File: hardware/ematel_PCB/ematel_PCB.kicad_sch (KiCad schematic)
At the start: 138 parts, among them J1 V_USB, J10 Micro_SD_Card, J11 HDR-4x1, J12 HDR-2x1, J13 HDR-2x1, J14 HDR-2x1, J15 HDR-2x1, J16 HDR-2x1, J17 USB_B_Micro, J2 BAT, J3 HDR-2x1, J4 IN, J5 HDR-3x1, J6 HDR-3x1, J7 IN, J8 HDR-2x1, J9 Conn_01x02, Q1 Q_PMOS_GSD, Q2 Q_PMOS_GSD, Q3 Q_Dual_NPN_NPN_BRT_E1B1C2E2B2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, SW1 SW_DIP_x02, SW3 SW_DIP_x02, SW4 SW_DIP_x02, U1 MAX3485, U10 AP2112K-3.3, U11 AP2112K-3.3, U12 ESP32-WROOM-32D, U13 RV-8803, U14 CH340C, U15 MCP23017_SO, U2 INA219AxD, U3 INA219AxD, U4 DW01, U5 TP4056, U6 MT3608, U7 FS8205A, U8 AP2112K-3.3, U9 LM2596S-5

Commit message: PCB update
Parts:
- added JP7, JP8, JP9: SolderJumper_2_Open, Jumper:SolderJumper-2_P1.3mm_Open_RoundedPad1.0x1.5mm, symbol Jumper:SolderJumper_2_Open
- added R49, R50: 10k, Resistor_SMD:R_0603_1608Metric, symbol IoWLabs:RES
- added R51, R52, R53, R54, R55, R56: 3.3k, Resistor_SMD:R_0603_1608Metric, symbol IoWLabs:RES
- R13, R14, R8, R9: value 4.7k -> 10k
- R17: value 10K -> 10k
- R43, R44: value 2.2k -> 10k
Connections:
- net +3V3: now also U15.9 (VDD), JP7.1 (A), JP8.1 (A), JP9.1 (A), R54.2, R55.2, R56.2
- net GND: now also U15.10 (VSS), R51.1, R52.1, R53.1
- net SCL: now also R50.1; no longer U15.12 (SCK)
- net SDA: now also R49.1; no longer U15.13 (SDA)
- net A0: now reaches U15.15 (A0)
- net A0: now also JP7.2 (B), R51.2
- net A1: now reaches U15.16 (A1)
- net A1: now also JP8.2 (B), R52.2
- net A2: now reaches U15.17 (A2)
- net A2: now also JP9.2 (B), R53.2
- net MCP_RESET: now reaches U15.18 (~{RESET})
- net MCP_RESET: now also R54.1
- net INTB: now reaches U15.19 (INTB)
- net INTB: now also R56.1
- net INTA: now reaches U15.20 (INTA)
- net INTA: now also R55.1
- new net: R50.2, U15.12 (SCK)
- new net: R49.2, U15.13 (SDA)
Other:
- note added: "MCP23017 IO EXTENSOR"
- moved on the sheet: U15

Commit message: Update PCB (Finish(?))
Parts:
- added C25, C26, C27: 0.1uF, Capacitor_SMD:C_0603_1608Metric, symbol IoWLabs:C
- added J15: Conn_01x04, Connector_JST:JST_XH_B3B-XH-A_1x03_P2.50mm_Vertical, symbol Connector_Generic:Conn_01x04
- added J16: Conn_01x08, Connector_JST:JST_XH_B3B-XH-A_1x03_P2.50mm_Vertical, symbol Connector_Generic:Conn_01x08
- added J20, J21, J22, J23: HDR-4x1, IoWLabsConnectors:TB-4x1-5P-TH-V, symbol IoWLabsConnectors:HDR-3x1
- added J24, J25, J26: Conn_01x02, Connector_JST:JST_XH_B3B-XH-A_1x03_P2.50mm_Vertical, symbol Connector_Generic:Conn_01x02
- added R46, R47, R48: 10k, Resistor_SMD:R_0603_1608Metric, symbol IoWLabs:RES
- added R49, R50, R51: 1k, Resistor_SMD:R_0603_1608Metric, symbol IoWLabs:RES
- added R52, R53, R54, R55: 10k2, Resistor_SMD:R_0603_1608Metric, symbol IoWLabs:RES
- added R56, R57, R58, R59: 3k3, Resistor_SMD:R_0603_1608Metric, symbol IoWLabs:RES
- C19: renamed from C8; footprint Capacitor_SMD:C_0603_1608Metric -> Capacitor_SMD:C_0805_2012Metric
- C20: renamed from C10; footprint Capacitor_SMD:C_0603_1608Metric -> Capacitor_SMD:C_0805_2012Metric
- C21: renamed from C11; footprint Capacitor_SMD:C_0603_1608Metric -> Capacitor_SMD:C_0805_2012Metric
- C22: renamed from C12; footprint Capacitor_SMD:C_0603_1608Metric -> Capacitor_SMD:C_0805_2012Metric
- C23: renamed from C13; footprint Capacitor_SMD:C_0603_1608Metric -> Capacitor_SMD:C_0805_2012Metric
- C24: renamed from C15; footprint Capacitor_SMD:C_0603_1608Metric -> Capacitor_SMD:C_0805_2012Metric
- R12: renamed from R20; value 1K -> 1k
- R2: renamed from R19; value 1K2 -> 1k2
- R20: renamed from R7; value 10K -> 10k
- R21: renamed from R12; value 10K -> 10k
- R22: renamed from R10; value 10K -> 10k
- R23: renamed from R15; value 10K -> 10k
- R24: renamed from R38; value 10K -> 10k
- R25: renamed from R39; value 10K -> 10k
- R27: renamed from R21; value 7K5 -> 7k5
- R29: renamed from R22; value 1K -> 1k
- R3: renamed from R23; value 12K -> 12k
- R36: renamed from R33; value 10K -> 10k
- R37: renamed from R34; value 10K -> 10k
- R39: renamed from R29; value 10K -> 10k
- R4: renamed from R25; value 30K -> 30k
- R41: renamed from R30; value 12K -> 12k
- R42: renamed from R31; value 30K -> 30k
- renumbered C6 to C1, C20 to C10, C7 to C11, C21 to C12, C9 to C13, C16 to C15, C24 to C16, C22 to C17, C23 to C18, C5 to C2, C17 to C3, C18 to C4, C4 to C5, C1 to C6, C2 to C7, C3 to C8, C19 to C9, D9 to D10, D6 to D11, D7 to D12, D8 to D13, D12 to D3, D3 to D6, D13 to D7, D10 to D8, D11 to D9, H3 to H2, H2 to H3, J2 to J1, J15 to J10, J7 to J11, J9 to J12, J17 to J13, J4 to J14, J10 to J17, J6 to J18, J5 to J19, J1 to J2, J12 to J3, J13 to J4, J11 to J5, J3 to J6, J16 to J7, J14 to J8, J8 to J9, Q3 to Q2, Q2 to Q3, R16 to R1, R18 to R10, R35 to R11, R8 to R13, R13 to R14, R9 to R15, R14 to R16, R6 to R18, R11 to R19, R37 to R26, R24 to R28, R36 to R30, R41 to R31, R42 to R32, R43 to R33, R44 to R34, R40 to R35, R32 to R38, R46 to R40, R47 to R43, R45 to R44, R48 to R45, R2 to R5, R3 to R6, R26 to R60, R27 to R61, R28 to R62, R49 to R63, R50 to R64, R54 to R65, R55 to R66, R56 to R67, R51 to R68, R52 to R69, R4 to R7, R53 to R70, R5 to R8, R1 to R9, U5 to U1, U9 to U10, U14 to U11, U8 to U12, U10 to U13, U11 to U14, U1 to U2, U4 to U3, U7 to U4, U12 to U5, U2 to U6, U3 to U7, U6 to U8, U13 to U9
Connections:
- net scl is gone; now on net SCL: R33.2
- net sda is gone; now on net SDA: R34.2
- net +3V3: now also R46.1, R47.1, R48.1
- net GND: now also C25.2, C26.2, C27.2, J20.2, J21.2, J22.2, J23.2, J24.2 (Pin_2), J25.2 (Pin_2), J26.2 (Pin_2), R56.1, R57.1, R58.1, R59.1
- net SD_CS: now also U5.29 (IO5)
- net SENSOR 1: now also R52.2, R56.2
- net SENSOR 2: now also U15.24 (GPA3), R53.2, R57.2; no longer U5.29 (IO5)
- net SENSOR 3: now also R54.2, R58.2
- net SENSOR 4: now also R55.2, R59.2
- net VIN_12V: now also J20.1, J21.1, J22.1, J23.1
- net GPB0: now reaches U15.1 (GPB0)
- net GPB0: now also J16.1 (Pin_1)
- net GPB1: now reaches U15.2 (GPB1)
- net GPB1: now also J16.2 (Pin_2)
- net GPA0: now reaches U15.21 (GPA0)
- net GPA0: now also C25.1, R46.2, R49.2
- net GPA1: now reaches U15.22 (GPA1)
- net GPA1: now also C26.1, R47.2, R50.2
- net GPA2: now reaches U15.23 (GPA2)
- net GPA2: now also C27.1, R48.2, R51.2
- net GPA4: now reaches U15.25 (GPA4)
- net GPA4: now also J15.1 (Pin_1)
- net GPA5: now reaches U15.26 (GPA5)
- net GPA5: now also J15.2 (Pin_2)
- net GPA6: now reaches U15.27 (GPA6)
- net GPA6: now also J15.3 (Pin_3)
- net GPA7: now reaches U15.28 (GPA7)
- net GPA7: now also J15.4 (Pin_4)
- net GPB2: now reaches U15.3 (GPB2)
- net GPB2: now also J16.3 (Pin_3)
- net GPB3: now reaches U15.4 (GPB3)
- net GPB3: now also J16.4 (Pin_4)
- net GPB4: now reaches U15.5 (GPB4)
- net GPB4: now also J16.5 (Pin_5)
- net GPB5: now reaches U15.6 (GPB5)
- net GPB5: now also J16.6 (Pin_6)
- net GPB6: now reaches U15.7 (GPB6)
- net GPB6: now also J16.7 (Pin_7)
- net GPB7: now reaches U15.8 (GPB7)
- net GPB7: now also J16.8 (Pin_8)
- net IO2 GPB renamed IO2
- new net: J24.1 (Pin_1), R49.1
- new net: J26.1 (Pin_1), R51.1
- new net: J25.1 (Pin_1), R50.1
- new net S1_IN: J20.3, R52.1
- new net S2_IN: J21.3, R53.1
- new net S3_IN: J22.3, R54.1
- new net S4_IN: J23.3, R55.1
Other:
- note added: "B1"
- note added: "B2"
- note added: "B3"
- note added: "CONECTORES GPIO EXT"
- note added: "CONECTORES PROTOCOLOS"
- note added: "CONECTORES SENSORES"
- note added: "DEBOUNCERS"
- note added: "Lista de pines: ---------------- io0 - BOOT io1 - Tx io2 - LED status io3 - Rx io4 - SENSOR 1 io5 - SD/CS io12 - KR2 io13 - KR1 io14 - KR3 io15 - RS485_EN io16 - 485_TX io17 - 485_RX io18 - SPI1_CLK io19 - SPI1_MISO io21 - SDA io22 - SCL io23 - SPI1_MOSI io25 - KC2 i026 - KC1 io27 - KR4 io32 - KC4 io33 - KC3 io34 - SENSOR 3 io35 - SENSOR 4 io36 - V_AUTO_LVL io39 - BAT_LVL"
- note removed: "CONECTORES"
- note removed: "Lista de pines: ---------------- io0 - BOOT io1 - Tx io2 - LED status io3 - Rx io4 - DO_LORA io5 - SD_CS io12 - SPI2_MISO io13 - SPI2_MOSI io14 - SPI2_CLK io15 - LORA_CS io16 - D1_LORA io17 - RST_LORA io18 - SPI1_CLK io19 - SPI1_MISO io21 - SDA/CS io22 - SCL/SCK io23 - SPI1_MOSI io25 - RST_GPS i026 - RGB_PIN io27 - EN_VDL io32 - EN_VS io33 - io34 - BTN1 io35 - BTN2 io36 - V_AUTO_LVL io39 - BAT_LVL"
- moved on the sheet: BT1, C12, C17, C18, C6, C7, D7, J12, J17, JP1, JP2, JP3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

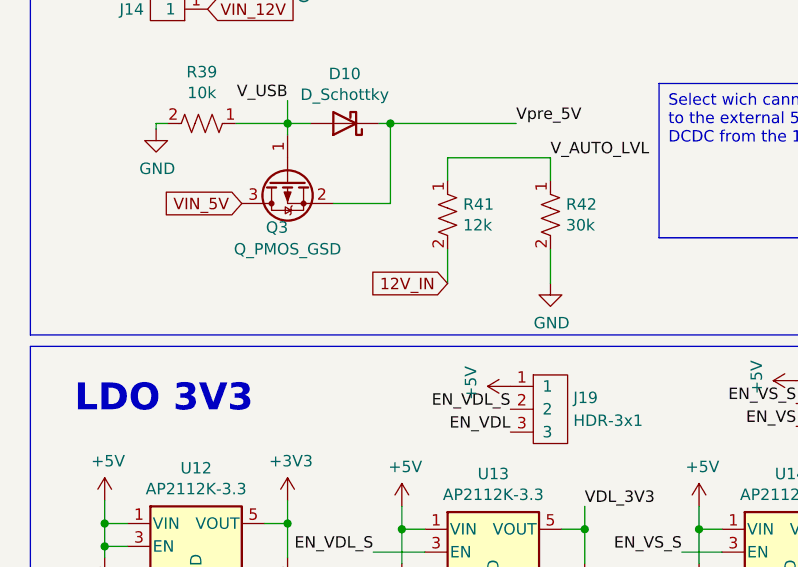
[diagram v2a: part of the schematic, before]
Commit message: PCB Update, layout begin
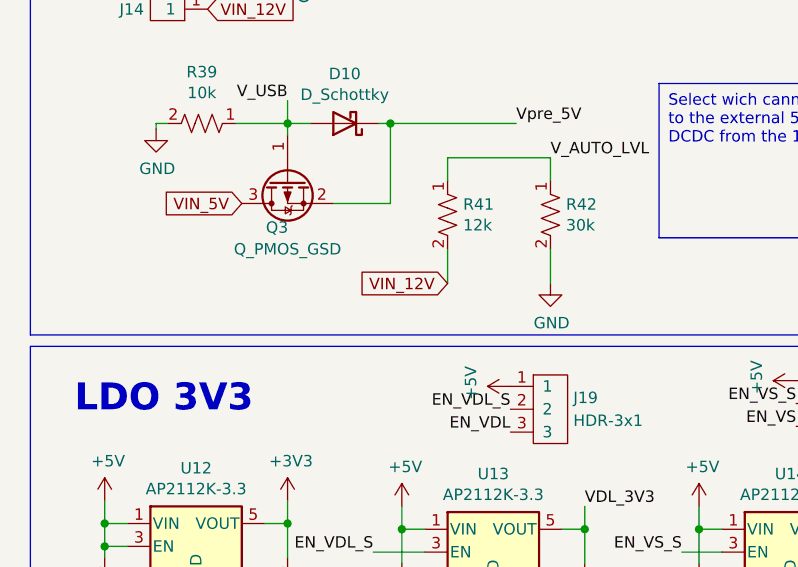
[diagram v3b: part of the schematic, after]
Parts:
- J15: footprint Connector_JST:JST_XH_B3B-XH-A_1x03_P2.50mm_Vertical -> Connector_JST:JST_XH_B4B-XH-AM_1x04_P2.50mm_Vertical
- J16: footprint Connector_JST:JST_XH_B3B-XH-A_1x03_P2.50mm_Vertical -> Connector_JST:JST_XH_B8B-XH-AM_1x08_P2.50mm_Vertical
- J24, J25, J26: footprint Connector_JST:JST_XH_B3B-XH-A_1x03_P2.50mm_Vertical -> Connector_JST:JST_XH_B2B-XH-AM_1x02_P2.50mm_Vertical
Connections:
- net 12V_IN: no longer R41.2
- net VIN_12V: now also R41.2
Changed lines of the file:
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@@
 		)
 	)
+	(global_label "VIN_12V"
+		(shape input)
+		(at 59.69 275.59 180)
+		(fields_autoplaced yes)
+		(effects
+			(font
+				(size 1.27 1.27)
+			)
+			(justify right)
+		)
+		(property "Intersheetrefs" "${INTERSHEET_REFS}"
+			(at 49.2057 275.59 0)
+			(effects
+				(font
+					(size 1.27 1.27)
+				)
+				(justify right)
+				(hide yes)
+			)
+		)
+	)
 	(global_label "RS485_B_ch2"
 		(shape input)
@@
 		)
 	)
-	(global_label "12V_IN"
-		(shape input)
-		(at 59.69 275.59 180)
-		(fields_autoplaced yes)
-		(effects
-			(font
-				(size 1.27 1.27)
-			)
-			(justify right)
-		)
-		(property "Intersheetrefs" "${INTERSHEET_REFS}"
-			(at 50.2943 275.59 0)
-			(effects
-				(font
-					(size 1.27 1.27)
-				)
-				(justify right)
-				(hide yes)
-			)
-		)
-	)
 	(global_label "KC2"
 		(shape input)
@@
 			)
 		)
-		(property "Footprint" "Connector_JST:JST_XH_B3B-XH-A_1x03_P2.50mm_Vertical"
+		(property "Footprint" "Connector_JST:JST_XH_B4B-XH-AM_1x04_P2.50mm_Vertical"
 			(at 389.89 248.92 0)
 			(effects
@@
 			)
 		)
-		(property "Footprint" "Connector_JST:JST_XH_B3B-XH-A_1x03_P2.50mm_Vertical"
+		(property "Footprint" "Connector_JST:JST_XH_B2B-XH-AM_1x02_P2.50mm_Vertical"
 			(at 370.84 311.15 0)
 			(effects
@@
 			)
 		)
-		(property "Footprint" "Connector_JST:JST_XH_B3B-XH-A_1x03_P2.50mm_Vertical"
+		(property "Footprint" "Connector_JST:JST_XH_B2B-XH-AM_1x02_P2.50mm_Vertical"
 			(at 425.45 311.15 0)
 			(effects
@@
 			)
 		)
-		(property "Footprint" "Connector_JST:JST_XH_B3B-XH-A_1x03_P2.50mm_Vertical"
+		(property "Footprint" "Connector_JST:JST_XH_B8B-XH-AM_1x08_P2.50mm_Vertical"
 			(at 370.84 254 0)
 			(effects
@@
 			)
 		)
-		(property "Footprint" "Connector_JST:JST_XH_B3B-XH-A_1x03_P2.50mm_Vertical"
+		(property "Footprint" "Connector_JST:JST_XH_B2B-XH-AM_1x02_P2.50mm_Vertical"
 			(at 398.78 311.15 0)
 			(effects
